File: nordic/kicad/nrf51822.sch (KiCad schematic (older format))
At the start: 19 parts, among them P1 CONN_01X04, X1 Crystal

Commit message: Added BALF antenna's footprint; added maching network's antenna circuit values
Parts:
- added U?: BALF-NRF01E3, LGA6S60X50P2X3_100X150X48, symbol BALF-NRF01E3
- C4: value C_Small -> 1pF
- C5: value C_Small -> 2.2pF
- C6: value C_Small -> 1.5pF
- L1: value L -> 4.7nH
- L2: value L -> 10nH
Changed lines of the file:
@@
 LIBS:valves
 LIBS:nrf51822
+LIBS:BALF-NRF01E3
 LIBS:nrf51822-cache
 EELAYER 25 0
@@
 P 8350 4050
 F 0 "L2" V 8300 4050 50  0000 C CNN
-F 1 "L" V 8425 4050 50  0000 C CNN
+F 1 "10nH" V 8425 4050 50  0000 C CNN
 F 2 "" H 8350 4050 50  0000 C CNN
 F 3 "" H 8350 4050 50  0000 C CNN
@@
 P 8350 3550
 F 0 "L1" V 8300 3550 50  0000 C CNN
-F 1 "L" V 8425 3550 50  0000 C CNN
+F 1 "4.7nH" V 8425 3550 50  0000 C CNN
 F 2 "" H 8350 3550 50  0000 C CNN
 F 3 "" H 8350 3550 50  0000 C CNN
@@
 P 8650 3300
 F 0 "C5" H 8660 3370 50  0000 L CNN
-F 1 "C_Small" H 8660 3220 50  0000 L CNN
+F 1 "2.2pF" H 8660 3220 50  0000 L CNN
 F 2 "" H 8650 3300 50  0000 C CNN
 F 3 "" H 8650 3300 50  0000 C CNN
@@
 P 9100 3500
 F 0 "C4" H 9110 3570 50  0000 L CNN
-F 1 "C_Small" H 9110 3420 50  0000 L CNN
+F 1 "1pF" H 9110 3420 50  0000 L CNN
 F 2 "" H 9100 3500 50  0000 C CNN
 F 3 "" H 9100 3500 50  0000 C CNN
@@
 P 9900 3500
 F 0 "C6" H 9910 3570 50  0000 L CNN
-F 1 "C_Small" H 9910 3420 50  0000 L CNN
+F 1 "1.5pF" H 9910 3420 50  0000 L CNN
 F 2 "" H 9900 3500 50  0000 C CNN
 F 3 "" H 9900 3500 50  0000 C CNN
@@
 Wire Wire Line
 	10450 3300 10450 2850
+$Comp
+L BALF-NRF01E3 U?
+U 1 1 592AEE8B
+P 9650 4800
+F 0 "U?" H 9250 5250 50  0000 L BNN
+F 1 "BALF-NRF01E3" H 9275 4275 50  0000 L BNN
+F 2 "LGA6S60X50P2X3_100X150X48" H 9650 4800 50  0001 L BNN
+F 3 "BALF-NRF01E3" H 9650 4800 50  0001 L BNN
+F 4 "0.30 USD" H 9650 4800 50  0001 L BNN "Price"
+F 5 "LGA-6 STMicroelectronics" H 9650 4800 50  0001 L BNN "Package"
+F 6 "STMicroelectronics" H 9650 4800 50  0001 L BNN "MF"
+F 7 "50%CE%A9 nominal input / conjugate match balun to nRF51x22-QFAA%2C nRF51x22-QFAC%2C nRF51822-QFABBx and nRF51422-QFABAx with i..." H 9650 4800 50  0001 L BNN "Description"
+F 8 "Good" H 9650 4800 50  0001 L BNN "Availability"
+	1    9650 4800
+	-1   0    0    1
+$EndComp
 $EndSCHEMATC

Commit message: Corrections in the antenna's matching network
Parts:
- removed C4: 1pF, symbol C_Small
- removed C5: 2.2pF, symbol C_Small
- removed C6: 1.5pF, symbol C_Small
- removed L1: 4.7nH, symbol L
- removed L2: 10nH, symbol L
- removed L3: L, symbol L
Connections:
- wire segments 65 -> 72
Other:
- moved on the sheet: AE1, C10, C8, U?

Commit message: PCB completo
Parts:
- BT1: footprint (none) -> nrf51822:cr2032_bat_holder
- C1, C10, C11, C2, C7, C9: footprint (none) -> Capacitors_SMD:C_0402
- C8: renamed from C3; footprint (none) -> Capacitors_SMD:C_0402
- C88: renamed from C8; footprint (none) -> Capacitors_SMD:C_0402
- P1: footprint (none) -> Pin_Headers:Pin_Header_Straight_1x04_Pitch2.00mm
- U1: renamed from U?; footprint LGA6S60X50P2X3_100X150X48 -> BALF-NRF01E3:LGA6S60X50P2X3_100X150X48
- X1: footprint (none) -> Crystals:Crystal_SMD_5032-2pin_5.0x3.2mm
- nRF51822: footprint (none) -> nrf51822:nRF51822
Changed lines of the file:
@@
 F 0 "nRF51822" H 6750 2550 60  0000 C CNN
 F 1 "nRF51822" H 5650 3850 60  0000 C CNN
-F 2 "" H 5150 4450 60  0001 C CNN
+F 2 "nrf51822:nRF51822" H 5150 4450 60  0001 C CNN
 F 3 "" H 5150 4450 60  0001 C CNN
 	1    5650 3850
@@
 F 0 "C7" H 3660 3170 50  0000 L CNN
 F 1 "C_Small" H 3300 3000 50  0000 L CNN
-F 2 "" H 3650 3100 50  0000 C CNN
+F 2 "Capacitors_SMD:C_0402" H 3650 3100 50  0001 C CNN
 F 3 "" H 3650 3100 50  0000 C CNN
 	1    3650 3100
@@
 F 0 "C11" H 3710 4870 50  0000 L CNN
 F 1 "C_Small" H 3710 4720 50  0000 L CNN
-F 2 "" H 3700 4800 50  0000 C CNN
+F 2 "Capacitors_SMD:C_0402" H 3700 4800 50  0001 C CNN
 F 3 "" H 3700 4800 50  0000 C CNN
 	1    3700 4800
@@
 F 0 "C10" H 7510 4170 50  0000 L CNN
 F 1 "C_Small" H 7510 4020 50  0000 L CNN
-F 2 "" H 7500 4100 50  0000 C CNN
+F 2 "Capacitors_SMD:C_0402" H 7500 4100 50  0001 C CNN
 F 3 "" H 7500 4100 50  0000 C CNN
 	1    7500 4100
@@
 $EndComp
 $Comp
-L C_Small C8
+L C_Small C88
 U 1 1 59262F55
 P 8200 4150
-F 0 "C8" H 8210 4220 50  0000 L CNN
+F 0 "C88" H 8210 4220 50  0000 L CNN
 F 1 "C_Small" H 8210 4070 50  0000 L CNN
-F 2 "" H 8200 4150 50  0000 C CNN
+F 2 "Capacitors_SMD:C_0402" H 8200 4150 50  0001 C CNN
 F 3 "" H 8200 4150 50  0000 C CNN
 	1    8200 4150
@@
 F 0 "C9" H 7710 2970 50  0000 L CNN
 F 1 "C_Small" H 7710 2820 50  0000 L CNN
-F 2 "" H 7700 2900 50  0000 C CNN
+F 2 "Capacitors_SMD:C_0402" H 7700 2900 50  0001 C CNN
 F 3 "" H 7700 2900 50  0000 C CNN
 	1    7700 2900
@@
 $EndComp
 $Comp
-L GND #PWR08
+L GND #PWR06
 U 1 1 59263FE2
 P 7700 3100
-F 0 "#PWR08" H 7700 2850 50  0001 C CNN
+F 0 "#PWR06" H 7700 2850 50  0001 C CNN
 F 1 "GND" H 7700 2950 50  0000 C CNN
 F 2 "" H 7700 3100 50  0000 C CNN
@@
 F 0 "X1" H 6450 1550 50  0000 C CNN
 F 1 "Crystal" H 6450 1250 50  0000 C CNN
-F 2 "" H 6450 1400 50  0000 C CNN
+F 2 "Crystals:Crystal_SMD_5032-2pin_5.0x3.2mm" H 6450 1400 50  0001 C CNN
 F 3 "" H 6450 1400 50  0000 C CNN
 	1    6450 1400
@@
 $EndComp
 $Comp
-L GND #PWR09
+L GND #PWR07
 U 1 1 5926CA36
 P 6450 900
-F 0 "#PWR09" H 6450 650 50  0001 C CNN
+F 0 "#PWR07" H 6450 650 50  0001 C CNN
 F 1 "GND" H 6450 750 50  0000 C CNN
 F 2 "" H 6450 900 50  0000 C CNN
@@
 F 0 "C2" H 6010 1120 50  0000 L CNN
 F 1 "C_Small" H 6010 970 50  0000 L CNN
-F 2 "" H 6000 1050 50  0000 C CNN
+F 2 "Capacitors_SMD:C_0402" H 6000 1050 50  0001 C CNN
 F 3 "" H 6000 1050 50  0000 C CNN
 	1    6000 1050
@@
 F 0 "C1" H 6810 1120 50  0000 L CNN
 F 1 "C_Small" H 6810 970 50  0000 L CNN
-F 2 "" H 6800 1050 50  0000 C CNN
+F 2 "Capacitors_SMD:C_0402" H 6800 1050 50  0001 C CNN
 F 3 "" H 6800 1050 50  0000 C CNN
 	1    6800 1050
@@
 $EndComp
 $Comp
-L C_Small C3
+L C_Small C8
 U 1 1 5926D284
 P 5600 1550
-F 0 "C3" H 5610 1620 50  0000 L CNN
+F 0 "C8" H 5610 1620 50  0000 L CNN
 F 1 "C_Small" H 5610 1470 50  0000 L CNN
-F 2 "" H 5600 1550 50  0000 C CNN
+F 2 "Capacitors_SMD:C_0402" H 5600 1550 50  0001 C CNN
 F 3 "" H 5600 1550 50  0000 C CNN
 	1    5600 1550
@@
 $EndComp
 $Comp
-L GND #PWR010
+L GND #PWR08
 U 1 1 5926D2E6
 P 5350 1550
-F 0 "#PWR010" H 5350 1300 50  0001 C CNN
+F 0 "#PWR08" H 5350 1300 50  0001 C CNN
 F 1 "GND" H 5350 1400 50  0000 C CNN
 F 2 "" H 5350 1550 50  0000 C CNN
@@
 F 0 "BT1" H 4500 6050 50  0000 L CNN
 F 1 "Battery" H 4500 5950 50  0000 L CNN
-F 2 "" V 4400 6010 50  0000 C CNN
+F 2 "nrf51822:cr2032_bat_holder" V 4400 6010 50  0000 C CNN
 F 3 "" V 4400 6010 50  0000 C CNN
 	1    4400 5950
@@
 NoConn ~ 5300 5250
 $Comp
-L PWR_FLAG #FLG011
+L PWR_FLAG #FLG09
 U 1 1 5928F042
 P 4050 5650
-F 0 "#FLG011" H 4050 5745 50  0001 C CNN
+F 0 "#FLG09" H 4050 5745 50  0001 C CNN
 F 1 "PWR_FLAG" H 4050 5830 50  0000 C CNN
 F 2 "" H 4050 5650 50  0000 C CNN
@@
 	7500 4000 7000 4000
 Wire Wire Line
-	7700 2600 7700 2750
-Wire Wire Line
-	7700 2750 7700 2800
-Wire Wire Line
-	7000 2750 7100 2750
-Wire Wire Line
-	7100 2750 7700 2750
+	7700 2600 7700 2800
+Wire Wire Line
+	7000 2750 7700 2750
 Wire Wire Line
 	7000 2750 7000 2950
@@
 	7000 3250 7200 3250
 Wire Wire Line
-	7200 3050 7200 3250
-Wire Wire Line
-	7200 3250 7200 3400
+	7200 3050 7200 3400
 Wire Wire Line
 	7200 3400 7000 3400
 Connection ~ 7200 3250
 Wire Wire Line
-	6000 950  6450 950
-Wire Wire Line
-	6450 950  6800 950
+	6000 950  6800 950
 Wire Wire Line
 	6450 900  6450 950
 Connection ~ 6450 950
 Wire Wire Line
-	6000 1150 6000 1400
-Wire Wire Line
-	6000 1400 6000 2000
+	6000 1150 6000 2000
 Wire Wire Line
 	6000 1400 6300 1400
 Wire Wire Line
-	6800 1150 6800 1400
-Wire Wire Line
-	6800 1400 6800 2000
+	6800 1150 6800 2000
 Wire Wire Line
 	6800 1400 6600 1400
@@
 Connection ~ 6000 1400
 Wire Wire Line
-	5350 1550 5400 1550
-Wire Wire Line
-	5400 1550 5500 1550
+	5350 1550 5500 1550
 Wire Wire Line
 	5700 1550 5950 1550
@@
 	6200 2100 6200 2350
 Wire Wire Line
-	3700 4450 3700 4600
-Wire Wire Line
-	3700 4600 3700 4700
+	3700 4450 3700 4700
 Wire Wire Line
 	3700 4600 4350 4600
 Connection ~ 3700 4600
 Wire Wire Line
-	4400 5550 4400 5700
-Wire Wire Line
-	4400 5700 4400 5750
+	4400 5550 4400 5750
 Wire Wire Line
 	6350 5250 6350 5700
@@
 	6500 5750 5150 5750
 Wire Wire Line
-	4050 5700 4400 5700
-Wire Wire Line
-	4400 5700 4950 5700
+	4050 5700 4950 5700
 Connection ~ 4400 5700
 Wire Wire Line
 	7200 3050 7700 3050
 Wire Wire Line
-	7700 3000 7700 3050
-Wire Wire Line
-	7700 3050 7700 3100
+	7700 3000 7700 3100
 Connection ~ 7700 3050
 Text GLabel 3700 4450 1    60   Input ~ 0
@@
 	4050 5650 4050 5700
 $Comp
-L PWR_FLAG #FLG012
+L PWR_FLAG #FLG010
 U 1 1 5929067A
 P 5400 1400
-F 0 "#FLG012" H 5400 1495 50  0001 C CNN
+F 0 "#FLG010" H 5400 1495 50  0001 C CNN
 F 1 "PWR_FLAG" H 5400 1580 50  0000 C CNN
 F 2 "" H 5400 1400 50  0000 C CNN
@@
 Connection ~ 5400 1550
 $Comp
-L GND #PWR013
+L GND #PWR011
 U 1 1 5929080D
 P 4400 6350
-F 0 "#PWR013" H 4400 6100 50  0001 C CNN
+F 0 "#PWR011" H 4400 6100 50  0001 C CNN
 F 1 "GND" H 4400 6200 50  0000 C CNN
 F 2 "" H 4400 6350 50  0000 C CNN
@@
 $EndComp
 Wire Wire Line
-	4400 6150 4400 6250
-Wire Wire Line
-	4400 6250 4400 6350
+	4400 6150 4400 6350
 Wire Wire Line
 	4850 6250 4400 6250
@@
 	3650 3350 3650 3200
 Wire Wire Line
-	3650 2700 3650 2950
-Wire Wire Line
-	3650 2950 3650 3000
+	3650 2700 3650 3000
 Wire Wire Line
 	3650 2950 4350 2950
@@
 F 0 "P1" H 5000 6700 50  0000 C CNN
 F 1 "CONN_01X04" V 5100 6450 50  0000 C CNN
-F 2 "" H 5000 6450 50  0000 C CNN
+F 2 "Pin_Headers:Pin_Header_Straight_1x04_Pitch2.00mm" H 5000 6450 50  0001 C CNN
 F 3 "" H 5000 6450 50  0000 C CNN
 	1    5000 6450
@@
 	9900 2950 9900 3650
 $Comp
-L BALF-NRF01E3 U?
+L BALF-NRF01E3 U1
 U 1 1 592AEE8B
 P 8950 3650
-F 0 "U?" H 8550 4100 50  0000 L BNN
+F 0 "U1" H 8550 4100 50  0000 L BNN
 F 1 "BALF-NRF01E3" H 8575 3125 50  0000 L BNN
-F 2 "LGA6S60X50P2X3_100X150X48" H 8950 3650 50  0001 L BNN
+F 2 "BALF-NRF01E3:LGA6S60X50P2X3_100X150X48" H 8950 3650 50  0001 L BNN
 F 3 "BALF-NRF01E3" H 8950 3650 50  0001 L BNN
 F 4 "0.30 USD" H 8950 3650 50  0001 L BNN "Price"
@@
 	8200 3950 8350 3950
 Wire Wire Line
-	8200 3850 8200 3950
-Wire Wire Line
-	8200 3950 8200 4050
+	8200 3850 8200 4050
 Wire Wire Line
 	8200 3850 7000 3850
@@
 Connection ~ 8200 3950
 $Comp
-L GND #PWR?
+L GND #PWR012
 U 1 1 592B023F
 P 8200 4500
-F 0 "#PWR?" H 8200 4250 50  0001 C CNN
+F 0 "#PWR012" H 8200 4250 50  0001 C CNN
 F 1 "GND" H 8200 4350 50  0000 C CNN
 F 2 "" H 8200 4500 50  0000 C CNN

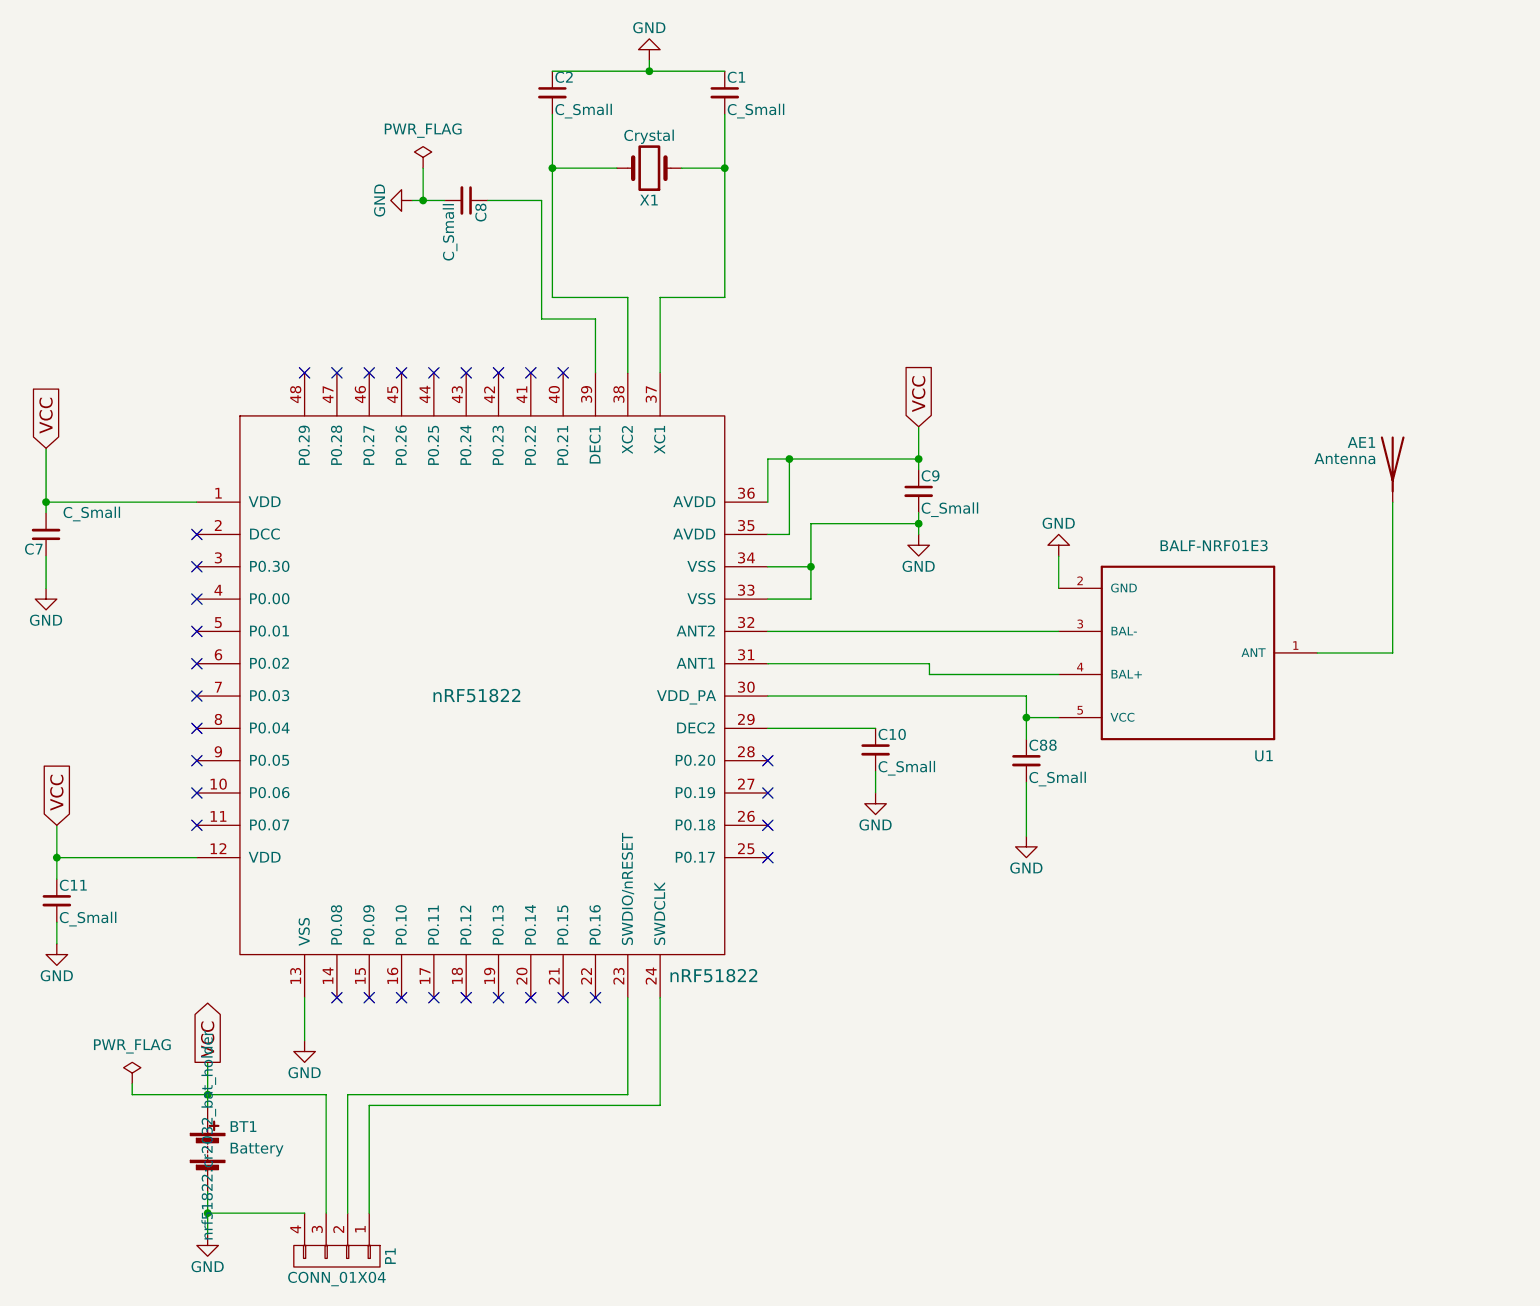
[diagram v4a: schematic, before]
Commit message: Adicionado pino pra anti-tampering, botão de reset e logo
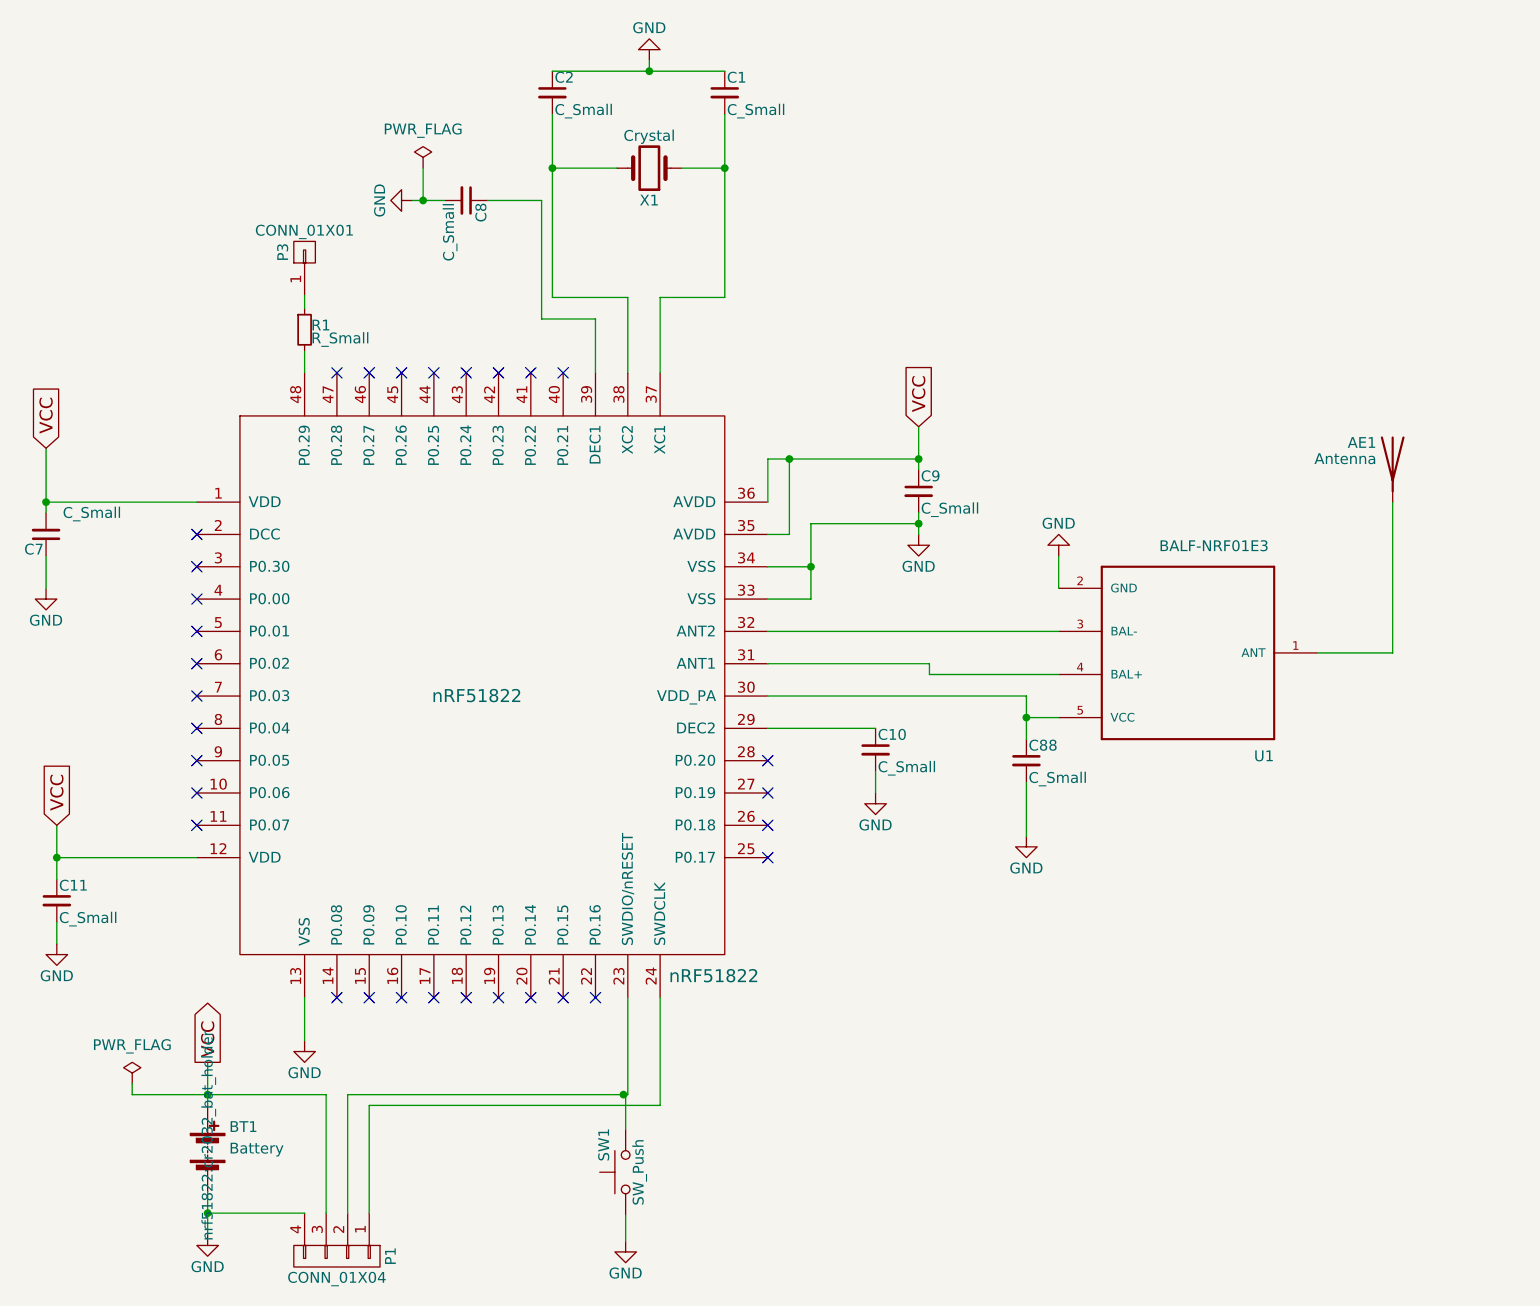
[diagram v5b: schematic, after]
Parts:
- added P3: CONN_01X01, Pin_Headers:Pin_Header_Straight_1x01_Pitch2.00mm, symbol CONN_01X01
- added R1: R_Small, Resistors_SMD:R_0402, symbol R_Small
- added SW1: SW_Push, Buttons_Switches_SMD:SW_SPST_TL3342, symbol SW_Push
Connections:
- net GND: now also SW1.1
- net at P1.2 (P2), nRF51822.23 (SWDIO/nRESET): now also SW1.2
- net at nRF51822.48 (P0.29): now also R1.2
- new net: P3.1 (P1), R1.1
- no-connect marks 32 -> 31
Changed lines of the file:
@@
 LIBS:nrf51822
 LIBS:BALF-NRF01E3
+LIBS:switches
 LIBS:nrf51822-cache
 EELAYER 25 0
@@
 encoding utf-8
 Sheet 1 1
-Title ""
-Date ""
-Rev ""
+Title "Beecon"
+Date "2017-05-08"
+Rev "0.1.4"
 Comp ""
 Comment1 ""
@@
 Comment4 ""
 $EndDescr
-$Comp
-L nRF51822 nRF51822
-U 1 1 5926221C
-P 5650 3850
-F 0 "nRF51822" H 6750 2550 60  0000 C CNN
-F 1 "nRF51822" H 5650 3850 60  0000 C CNN
-F 2 "nrf51822:nRF51822" H 5150 4450 60  0001 C CNN
-F 3 "" H 5150 4450 60  0001 C CNN
-	1    5650 3850
-	1    0    0    -1
-$EndComp
 $Comp
 L GND #PWR1
@@
 $EndComp
 $Comp
-L GND #PWR7
+L GND #PWR8
 U 1 1 59262EC9
 P 7500 4300
-F 0 "#PWR7" H 7500 4050 50  0001 C CNN
+F 0 "#PWR8" H 7500 4050 50  0001 C CNN
 F 1 "GND" H 7500 4150 50  0000 C CNN
 F 2 "" H 7500 4300 50  0000 C CNN
@@
 $EndComp
 $Comp
-L GND #PWR10
+L GND #PWR11
 U 1 1 59262F8A
 P 8350 3200
-F 0 "#PWR10" H 8350 2950 50  0001 C CNN
+F 0 "#PWR11" H 8350 2950 50  0001 C CNN
 F 1 "GND" H 8350 3050 50  0000 C CNN
 F 2 "" H 8350 3200 50  0000 C CNN
@@
 $EndComp
 $Comp
-L GND #PWR8
+L GND #PWR9
 U 1 1 59263FE2
 P 7700 3100
-F 0 "#PWR8" H 7700 2850 50  0001 C CNN
+F 0 "#PWR9" H 7700 2850 50  0001 C CNN
 F 1 "GND" H 7700 2950 50  0000 C CNN
 F 2 "" H 7700 3100 50  0000 C CNN
@@
 $EndComp
 $Comp
-L GND #PWR6
+L GND #PWR7
 U 1 1 5926CA36
 P 6450 900
-F 0 "#PWR6" H 6450 650 50  0001 C CNN
+F 0 "#PWR7" H 6450 650 50  0001 C CNN
 F 1 "GND" H 6450 750 50  0000 C CNN
 F 2 "" H 6450 900 50  0000 C CNN
@@
 	1    0    0    -1
 $EndComp
-NoConn ~ 4850 2350
 NoConn ~ 5000 2350
 NoConn ~ 5150 2350
@@
 Wire Wire Line
 	3700 4450 3700 4700
-Wire Wire Line
-	3700 4600 4350 4600
 Connection ~ 3700 4600
 Wire Wire Line
 	4400 5550 4400 5750
 Wire Wire Line
-	6350 5250 6350 5700
-Wire Wire Line
-	6350 5700 5050 5700
+	6350 5700 6350 5250
+Wire Wire Line
+	5050 5700 6350 5700
 Wire Wire Line
 	6500 5750 5150 5750
@@
 Connection ~ 8200 3950
 $Comp
-L GND #PWR9
+L GND #PWR10
 U 1 1 592B023F
 P 8200 4500
-F 0 "#PWR9" H 8200 4250 50  0001 C CNN
+F 0 "#PWR10" H 8200 4250 50  0001 C CNN
 F 1 "GND" H 8200 4350 50  0000 C CNN
 F 2 "" H 8200 4500 50  0000 C CNN
@@
 Wire Wire Line
 	9900 3650 9550 3650
+$Comp
+L SW_Push SW1
+U 1 1 59399148
+P 6340 6060
+F 0 "SW1" H 6390 6160 50  0000 L CNN
+F 1 "SW_Push" H 6340 6000 50  0000 C CNN
+F 2 "Buttons_Switches_SMD:SW_SPST_TL3342" H 6340 6260 50  0001 C CNN
+F 3 "" H 6340 6260 50  0000 C CNN
+	1    6340 6060
+	0    -1   -1   0
+$EndComp
+Wire Wire Line
+	6340 5860 6340 5700
+Wire Wire Line
+	6340 5700 6330 5700
+Connection ~ 6330 5700
+$Comp
+L GND #PWR6
+U 1 1 593992D9
+P 6340 6380
+F 0 "#PWR6" H 6340 6130 50  0001 C CNN
+F 1 "GND" H 6340 6230 50  0000 C CNN
+F 2 "" H 6340 6380 50  0000 C CNN
+F 3 "" H 6340 6380 50  0000 C CNN
+	1    6340 6380
+	1    0    0    -1
+$EndComp
+Wire Wire Line
+	6340 6380 6340 6260
+$Comp
+L nRF51822 nRF51822
+U 1 1 5926221C
+P 5650 3850
+F 0 "nRF51822" H 6750 2550 60  0000 C CNN
+F 1 "nRF51822" H 5650 3850 60  0000 C CNN
+F 2 "nrf51822:nRF51822" H 5150 4450 60  0001 C CNN
+F 3 "" H 5150 4450 60  0001 C CNN
+	1    5650 3850
+	1    0    0    -1
+$EndComp
+$Comp
+L R_Small R1
+U 1 1 5939CCF8
+P 4850 2150
+F 0 "R1" H 4880 2170 50  0000 L CNN
+F 1 "R_Small" H 4880 2110 50  0000 L CNN
+F 2 "Resistors_SMD:R_0402" H 4850 2150 50  0001 C CNN
+F 3 "" H 4850 2150 50  0000 C CNN
+	1    4850 2150
+	1    0    0    -1
+$EndComp
+Wire Wire Line
+	4850 2350 4850 2250
+$Comp
+L CONN_01X01 P3
+U 1 1 5939DBBE
+P 4850 1790
+F 0 "P3" H 4850 1890 50  0000 C CNN
+F 1 "CONN_01X01" V 4950 1790 50  0000 C CNN
+F 2 "Pin_Headers:Pin_Header_Straight_1x01_Pitch2.00mm" H 4850 1790 50  0001 C CNN
+F 3 "" H 4850 1790 50  0000 C CNN
+	1    4850 1790
+	0    -1   -1   0
+$EndComp
+Wire Wire Line
+	4850 2050 4850 1990
+Wire Wire Line
+	3700 4600 4350 4600
 $EndSCHEMATC
